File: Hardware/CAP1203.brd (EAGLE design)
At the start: 38.1 x 25.4 mm, 44 parts, among them J1 Qwiic Right Angle, J2 Qwiic Right Angle, J3 Cap Touch Breakout Pins, J4 I2C Breakout Pins, U2 CAP1203

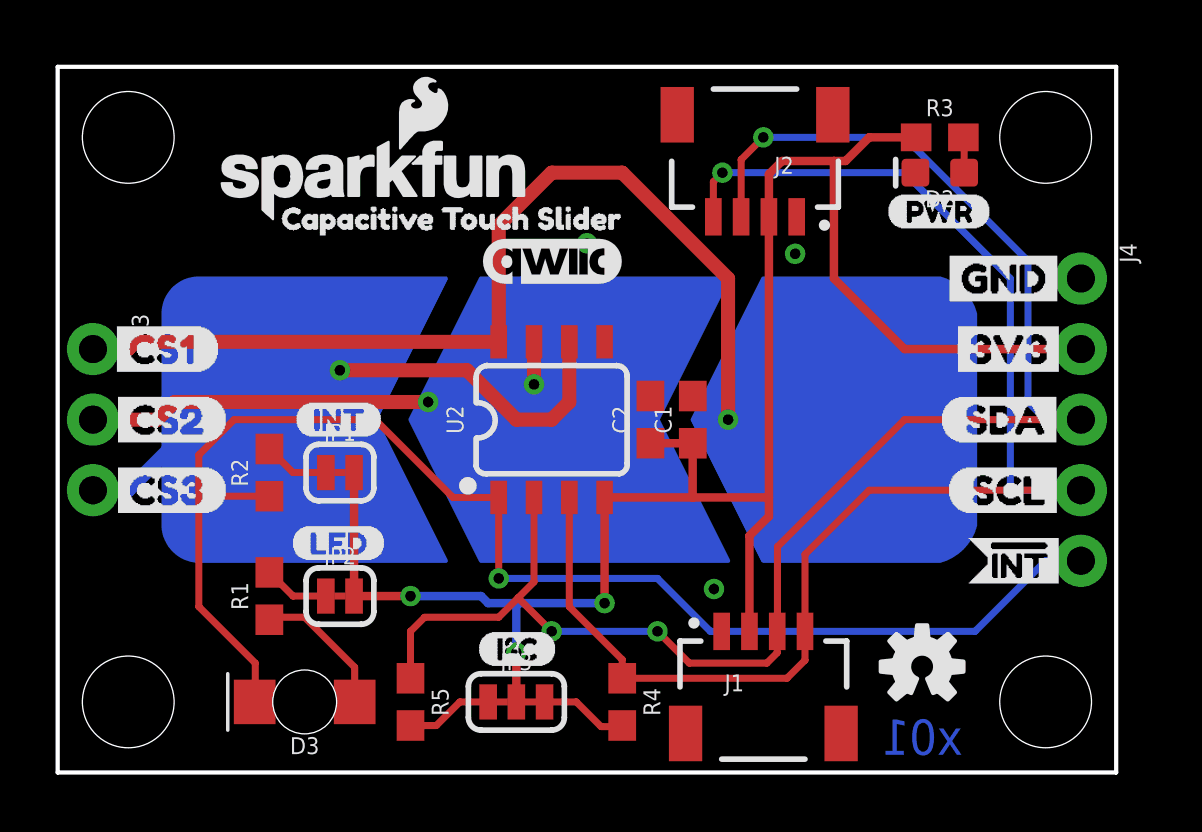
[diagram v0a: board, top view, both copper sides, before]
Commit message: Added CAP1203 from SparkFun library
* Replaced current CAP1203 with SparkFun library version
* Updated in both sch and brd files
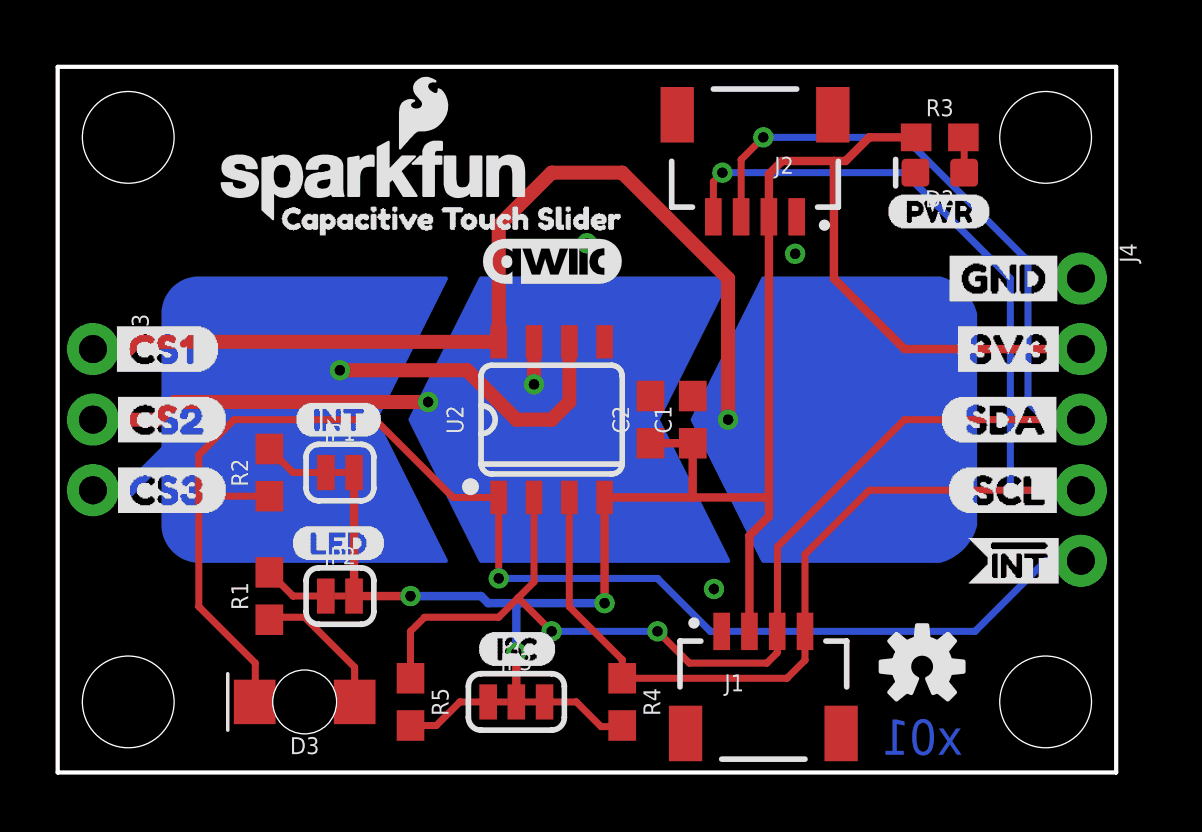
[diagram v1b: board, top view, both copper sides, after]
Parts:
- U2: device SparkX:SO08 -> SparkFun-Sensors:SO08-TIGHT
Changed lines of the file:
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@@
 <attribute name="VALUE" x="34.798" y="19.05" size="0.6096" layer="27" font="vector" ratio="20" rot="R270"/>
 </element>
-<element name="U2" library="SparkX" package="SO08" value="CAP1203" x="17.78" y="12.7" smashed="yes">
+<element name="U2" library="SparkFun-Sensors" package="SO08-TIGHT" value="CAP1203" x="17.78" y="12.7" smashed="yes">
 <attribute name="NAME" x="14.605" y="12.7" size="0.6096" layer="25" font="vector" ratio="20" rot="R90" align="bottom-center"/>
 <attribute name="PROD_ID" value="IC-14356" x="17.78" y="12.7" size="1.778" layer="27" display="off"/>

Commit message: Updated CAP1203 for production
* Moved PTH for capactive touch
* Updated traces accordingly
* Enlarged and moved labels
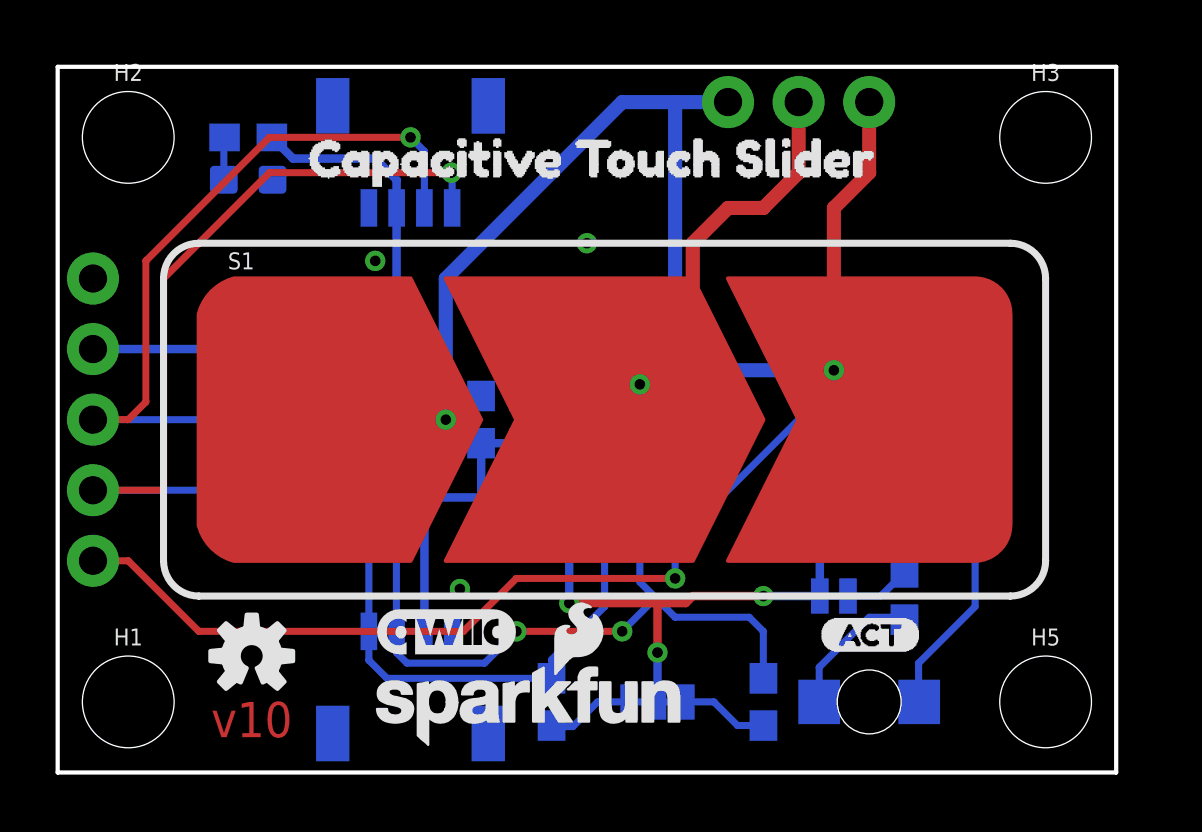
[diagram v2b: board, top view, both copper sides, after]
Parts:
- removed U$3, U$5: (no value), buzzard_labels_title:CAPACITIVE_TOUCH_SLIDER0
- added U$18: (no value), buzzard_labels (10):CAPACITIVE_TOUCH_SLIDER0
- added U$19: (no value), buzzard_labels (12):CAPACITIVE_TOUCH_SLIDER0
- moved FRAME1 48.3 mm to (43.2, -17.8), flipped to the bottom
- moved J4 35.6 mm to (1.27, 17.8), flipped to the bottom
- moved H1 33.0 mm to (2.54, 2.54), flipped to the top
- moved H2 33.0 mm to (2.54, 22.9), flipped to the top
- moved H3 33.0 mm to (35.6, 22.9), flipped to the top
- moved H5 33.0 mm to (35.6, 2.54), flipped to the top
- moved U$12 30.7 mm to (29.2, 23.7), flipped to the bottom, turned to 270 degrees
- moved U$11 27.4 mm to (26.7, 23.7), flipped to the bottom, turned to 270 degrees
- moved U$7 26.9 mm to (5.59, 7.62), flipped to the bottom
- moved U$8 25.9 mm to (6.10, 10.2), flipped to the bottom
- moved U$1 25.7 mm to (6.22, 15.2), flipped to the bottom
- moved U$9 25.4 mm to (6.35, 12.7), flipped to the bottom
- moved U$2 25.1 mm to (6.48, 17.8), flipped to the bottom
- moved D2 24.9 mm to (6.86, 21.3), flipped to the bottom
- moved R3 24.9 mm to (6.86, 22.9), flipped to the bottom
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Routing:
- net CS1: track 38.4 -> 30.3 mm
- net CS2: track 24.3 -> 16.5 mm, vias 2 -> 1
- net 3.3V: track 67.1 -> 62.6 mm
- net CS3: track 22.4 -> 24.9 mm
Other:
- board text added: "v10"
- board text removed: "x01"

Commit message: Removed wire stub
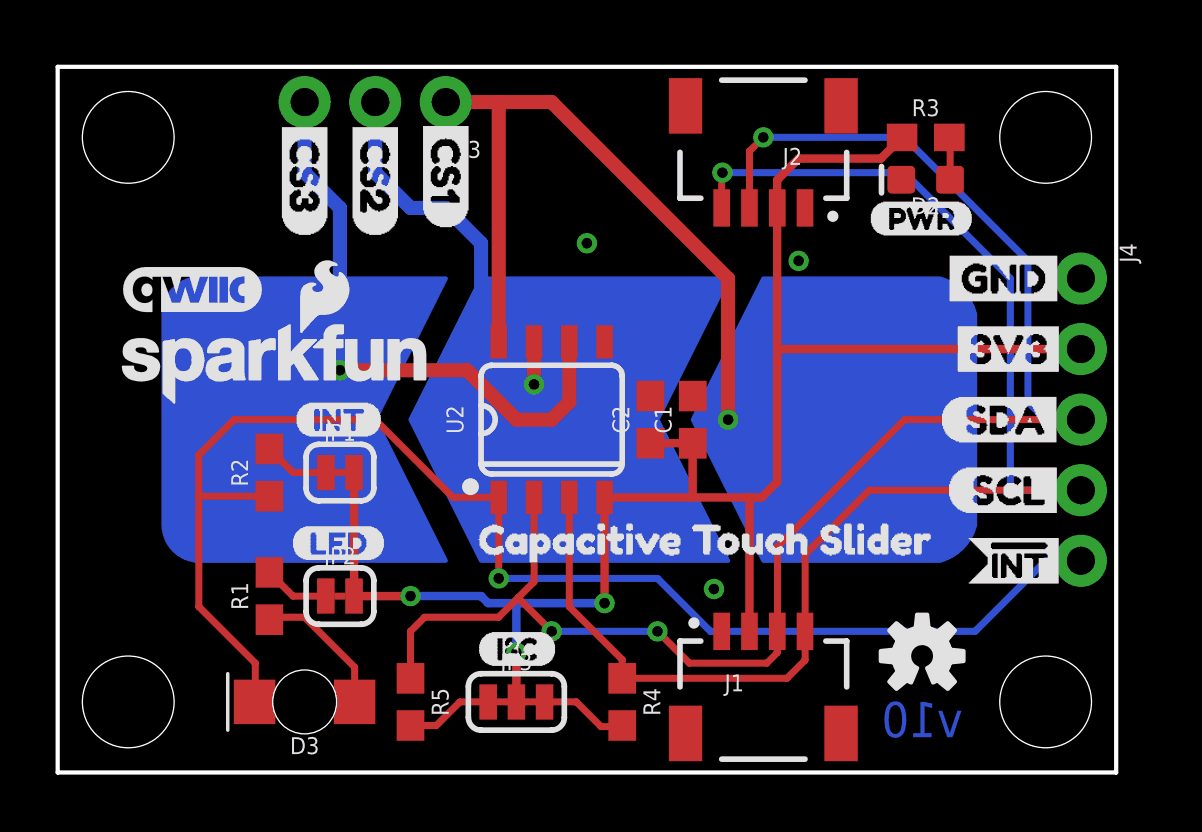
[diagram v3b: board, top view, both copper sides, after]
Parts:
- moved FRAME1 48.3 mm to (-5.08, -17.8), flipped to the top
- moved J4 35.6 mm to (36.8, 17.8), flipped to the top
- moved H1 33.0 mm to (35.6, 2.54), flipped to the bottom
- moved H2 33.0 mm to (35.6, 22.9), flipped to the bottom
- moved H3 33.0 mm to (2.54, 22.9), flipped to the bottom
- moved H5 33.0 mm to (2.54, 2.54), flipped to the bottom
- moved U$17 28.4 mm to (4.83, 17.4), flipped to the top
- moved U$7 26.9 mm to (32.5, 7.62), flipped to the top
- moved U$8 25.9 mm to (32.0, 10.2), flipped to the top
- moved U$1 25.7 mm to (31.9, 15.2), flipped to the top
- moved U$9 25.4 mm to (31.8, 12.7), flipped to the top
- moved U$2 25.1 mm to (31.6, 17.8), flipped to the top
- moved D2 24.4 mm to (31.2, 21.3), flipped to the top
- moved R3 24.4 mm to (31.2, 22.9), flipped to the top
- moved LOGO3 24.1 mm to (31.1, 4.19), flipped to the bottom
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
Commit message: Removed wire stub (correct now)
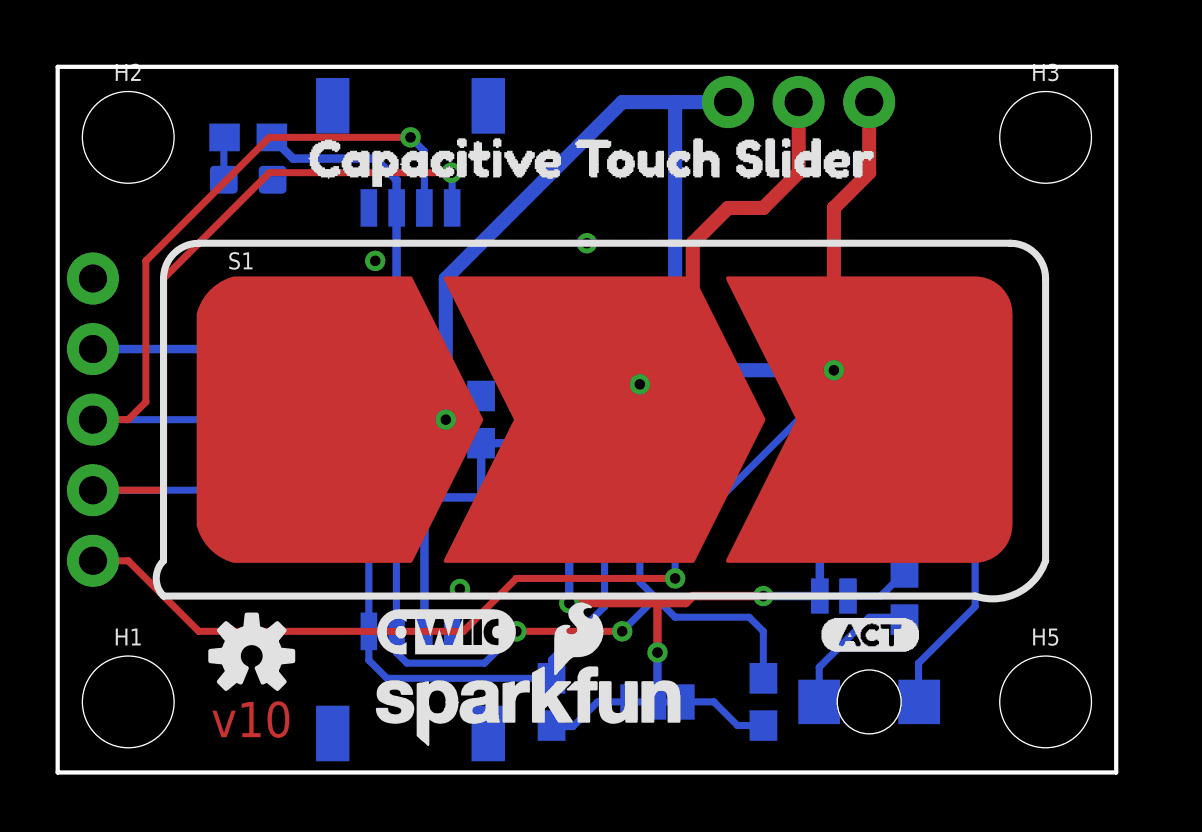
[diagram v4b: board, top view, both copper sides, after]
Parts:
- moved FRAME1 48.3 mm to (43.2, -17.8), flipped to the bottom
- moved J4 35.6 mm to (1.27, 17.8), flipped to the bottom
- moved H1 33.0 mm to (2.54, 2.54), flipped to the top
- moved H2 33.0 mm to (2.54, 22.9), flipped to the top
- moved H3 33.0 mm to (35.6, 22.9), flipped to the top
- moved H5 33.0 mm to (35.6, 2.54), flipped to the top
- moved U$17 28.4 mm to (33.3, 17.4), flipped to the bottom
- moved U$7 26.9 mm to (5.59, 7.62), flipped to the bottom
- moved U$8 25.9 mm to (6.10, 10.2), flipped to the bottom
- moved U$1 25.7 mm to (6.22, 15.2), flipped to the bottom
- moved U$9 25.4 mm to (6.35, 12.7), flipped to the bottom
- moved U$2 25.1 mm to (6.48, 17.8), flipped to the bottom
- moved D2 24.4 mm to (6.86, 21.3), flipped to the bottom
- moved R3 24.4 mm to (6.86, 22.9), flipped to the bottom
- moved LOGO3 24.1 mm to (6.99, 4.19), flipped to the top
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
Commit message: Fixed border
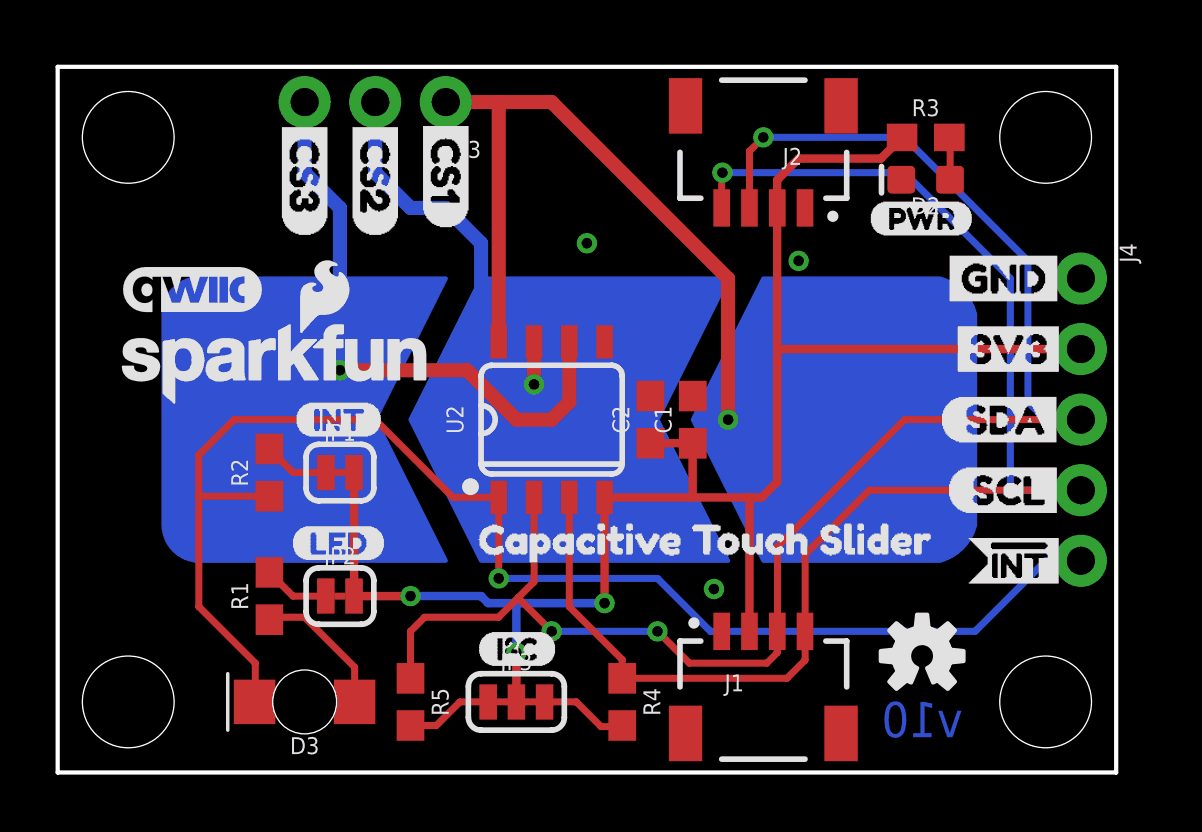
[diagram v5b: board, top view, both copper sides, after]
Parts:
- moved FRAME1 48.3 mm to (-5.08, -17.8), flipped to the top
- moved J4 35.6 mm to (36.8, 17.8), flipped to the top
- moved H1 33.0 mm to (35.6, 2.54), flipped to the bottom
- moved H2 33.0 mm to (35.6, 22.9), flipped to the bottom
- moved H3 33.0 mm to (2.54, 22.9), flipped to the bottom
- moved H5 33.0 mm to (2.54, 2.54), flipped to the bottom
- moved U$17 28.4 mm to (4.83, 17.4), flipped to the top
- moved U$7 26.9 mm to (32.5, 7.62), flipped to the top
- moved U$8 25.9 mm to (32.0, 10.2), flipped to the top
- moved U$1 25.7 mm to (31.9, 15.2), flipped to the top
- moved U$9 25.4 mm to (31.8, 12.7), flipped to the top
- moved U$2 25.1 mm to (31.6, 17.8), flipped to the top
- moved D2 24.4 mm to (31.2, 21.3), flipped to the top
- moved R3 24.4 mm to (31.2, 22.9), flipped to the top
- moved LOGO3 24.1 mm to (31.1, 4.19), flipped to the bottom
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
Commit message: Fixed silkscreen and labels
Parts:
- removed LOGO5: OSHW-LOGOS, SparkFun-Aesthetics:OSHW-LOGO-S
- removed U$19: (no value), buzzard_labels (12):CAPACITIVE_TOUCH_SLIDER0
- removed U$6: (no value), buzzard_labels (5):ACT0
- added U$5: (no value), buzzard_labels (4):INT0
- moved U$16 0.25 mm to (8.38, 8.00)
- moved U$13 0.25 mm to (15.1, 4.19)
- moved U$14 0.25 mm to (8.51, 12.4)
- moved U$15 0.13 mm to (29.2, 19.8)
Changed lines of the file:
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@@
 <element name="U$11" library="buzzard_labels-CAP1203" package="CS21" value="" x="11.43" y="23.749" smashed="yes" rot="R270"/>
 <element name="U$12" library="buzzard_labels-CAP1203" package="CS32" value="" x="8.89" y="23.749" smashed="yes" rot="R270"/>
-<element name="U$16" library="buzzard_labels (1)" package="LED0" value="" x="8.382" y="8.255" smashed="yes"/>
+<element name="U$16" library="buzzard_labels (1)" package="LED0" value="" x="8.382" y="8.001" smashed="yes"/>
 <element name="LOGO1" library="SparkFun-Aesthetics" package="SFE_LOGO_NAME_FLAME_.1" value="SFE_LOGO_NAME_FLAME.1_INCH" x="7.874" y="14.732" smashed="yes"/>
 <element name="LOGO3" library="SparkFun-Aesthetics" package="OSHW-LOGO-S" value="OSHW-LOGOS" x="31.115" y="4.191" smashed="yes" rot="MR0"/>
-<element name="LOGO5" library="SparkFun-Aesthetics" package="OSHW-LOGO-S" value="OSHW-LOGOS" x="31.115" y="4.191" smashed="yes"/>
 <element name="LOGO2" library="SparkFun-Aesthetics" package="SFE_LOGO_NAME_FLAME_.1" value="SFE_LOGO_NAME_FLAME.1_INCH" x="21.082" y="2.413" smashed="yes" rot="MR0"/>
-<element name="U$13" library="Labels" package="I_SUPER2_C-()-03" value="" x="15.113" y="4.445" smashed="yes"/>
-<element name="U$14" library="buzzard_labels (4)" package="INT0" value="" x="8.509" y="12.7" smashed="yes"/>
-<element name="U$15" library="Labels" package="PWR-()-03" value="" x="29.21" y="19.939" smashed="yes"/>
+<element name="U$13" library="Labels" package="I_SUPER2_C-()-03" value="" x="15.113" y="4.191" smashed="yes"/>
+<element name="U$14" library="buzzard_labels (4)" package="INT0" value="" x="8.509" y="12.446" smashed="yes"/>
+<element name="U$15" library="Labels" package="PWR-()-03" value="" x="29.21" y="19.812" smashed="yes"/>
 <element name="U$17" library="SparkFun-Aesthetics" package="QWIIC_5MM" value="QWIIC_LOGO_5MM" x="4.826" y="17.399" smashed="yes"/>
 <element name="U$4" library="SparkFun-Aesthetics" package="QWIIC_5MM" value="QWIIC_LOGO_5MM" x="24.13" y="5.08" smashed="yes" rot="MR0"/>
-<element name="U$6" library="buzzard_labels (5)" package="ACT0" value="" x="10.668" y="4.953" smashed="yes" rot="MR0"/>
 <element name="S1" library="SparkX" package="CAP_SENSE_SLIDER" value="" x="17.78" y="12.7" smashed="yes" rot="MR0">
 <attribute name="NAME" x="31.496" y="18.415" size="0.6096" layer="26" ratio="20" rot="MR0" align="center"/>
@@
 </element>
 <element name="U$18" library="buzzard_labels (10)" package="CAPACITIVE_TOUCH_SLIDER0" value="" x="30.226" y="21.463" smashed="yes" rot="MR0"/>
-<element name="U$19" library="buzzard_labels (12)" package="CAPACITIVE_TOUCH_SLIDER0" value="" x="14.224" y="8.382" smashed="yes"/>
+<element name="U$5" library="buzzard_labels (4)" package="INT0" value="" x="10.541" y="4.953" smashed="yes" rot="MR0"/>
 </elements>
 <signals>
@@
 <wire x1="36.83" y1="15.24" x2="25.9" y2="15.24" width="0.3048" layer="1"/>
 <wire x1="26.67" y1="22.098" x2="25.9" y2="21.328" width="0.3048" layer="1"/>
-<wire x1="12.7" y1="6.35" x2="10.6934" y2="6.35" width="0.3048" layer="1"/>
-<wire x1="10.6934" y1="6.35" x2="10.668" y2="6.35" width="0" layer="19" extent="16-16"/>
+<wire x1="10.668" y1="6.35" x2="12.7" y2="6.35" width="0.3048" layer="1"/>
 </signal>
 <signal name="N$1">
@@
 <mfgpreviewcolor name="substratecolor" color="0xFF786E46"/>
 </mfgpreviewcolors>
+<errors>
+</errors>
 </board>
 </drawing>
